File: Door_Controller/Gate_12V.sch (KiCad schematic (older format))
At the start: 6 parts

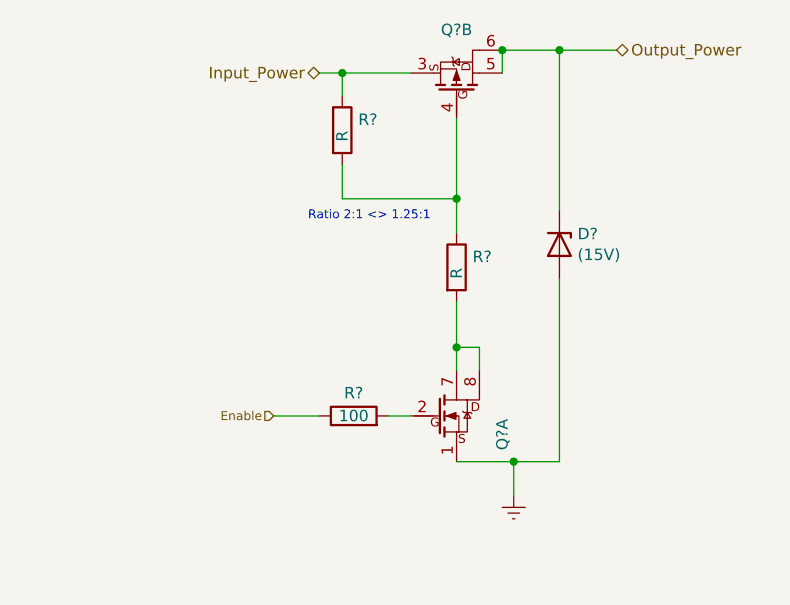
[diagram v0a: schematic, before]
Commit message: add filter caps to motor drive
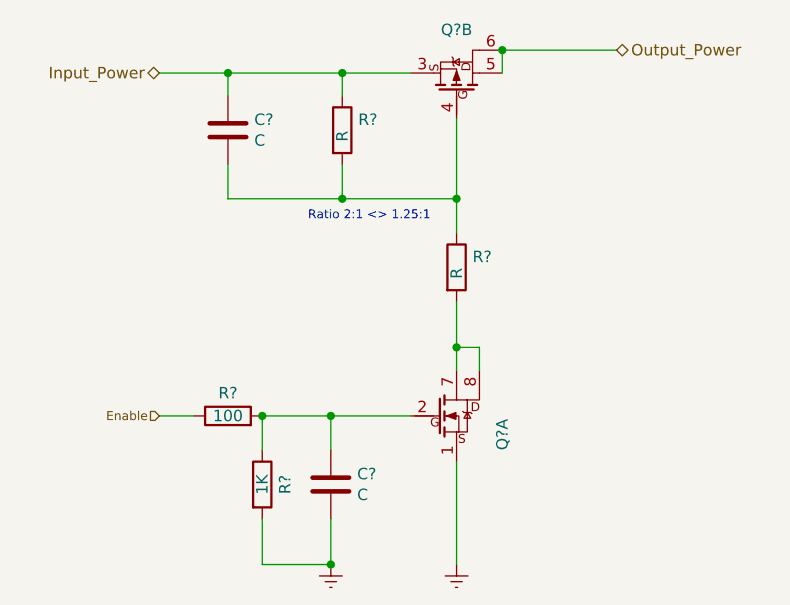
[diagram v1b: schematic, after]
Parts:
- removed D?: (15V), symbol Device:D_Zener
- added C? (x2): C, symbol Device:C
- added R?: 1K, symbol Device:R
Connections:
- net Earth: now also C?.2, R?.2
- net Input_Power: now also C?.1
- net at Q?.4, R?.1, R?.2: now also C?.2
- net at Q?.2, R?.2: now also C?.1, R?.1
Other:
- moved on the sheet: R?
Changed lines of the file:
@@
 $Descr A4 11693 8268
 encoding utf-8
-Sheet 7 14
+Sheet 8 14
 Title ""
 Date ""
@@
 Wire Wire Line
 	5200 2550 5200 2450
-Wire Wire Line
-	5200 2450 5450 2450
 Connection ~ 5200 2450
 $Comp
@@
 F 3 "~" H 4500 2800 50  0001 C CNN
 	1    4500 2800
+	1    0    0    -1
+$EndComp
+Text HLabel 3700 2550 0    50   BiDi ~ 0
+Input_Power
+Wire Wire Line
+	3700 2550 4000 2550
+Wire Wire Line
+	4500 2650 4500 2550
+Connection ~ 4500 2550
+Wire Wire Line
+	4500 2550 4800 2550
+Wire Wire Line
+	5000 3550 5000 3750
+Wire Wire Line
+	5100 3850 5100 3750
+Wire Wire Line
+	5100 3750 5000 3750
+Connection ~ 5000 3750
+Wire Wire Line
+	5000 3750 5000 3850
+Wire Wire Line
+	5000 2750 5000 3100
+Wire Wire Line
+	4500 2950 4500 3100
+Wire Wire Line
+	4500 3100 5000 3100
+Connection ~ 5000 3100
+Wire Wire Line
+	5000 3100 5000 3250
+$Comp
+L Device:R R?
+U 1 1 6066CE35
+P 5000 3400
+AR Path="/5FB4C28C/6066CE35" Ref="R?"  Part="1"
+AR Path="/5FB4C28C/606144ED/6066CE35" Ref="R?"  Part="1"
+AR Path="/5FB4C28C/60669CB5/6066CE35" Ref="R?"  Part="1"
+AR Path="/5FB4C28C/60BA7C5A/6066CE35" Ref="R?"  Part="1"
+F 0 "R?" H 5070 3446 50  0000 L CNN
+F 1 "R" V 5000 3350 50  0000 L CNN
+F 2 "" V 4930 3400 50  0001 C CNN
+F 3 "~" H 5000 3400 50  0001 C CNN
+	1    5000 3400
+	1    0    0    -1
+$EndComp
+Text Notes 4350 3200 0    39   ~ 0
+Ratio 2:1 <> 1.25:1
+Text HLabel 5700 2450 2    50   BiDi ~ 0
+Output_Power
+Wire Wire Line
+	5200 2450 5700 2450
+$Comp
+L power:Earth #PWR?
+U 1 1 6066DAA4
+P 5000 4700
+AR Path="/5FB4C28C/60669CB5/6066DAA4" Ref="#PWR?"  Part="1"
+AR Path="/5FB4C28C/60BA7C5A/6066DAA4" Ref="#PWR?"  Part="1"
+F 0 "#PWR?" H 5000 4450 50  0001 C CNN
+F 1 "Earth" H 5000 4550 50  0001 C CNN
+F 2 "" H 5000 4700 50  0001 C CNN
+F 3 "~" H 5000 4700 50  0001 C CNN
+	1    5000 4700
+	1    0    0    -1
+$EndComp
+Wire Wire Line
+	5000 4700 5000 4250
+$Comp
+L Device:C C?
+U 1 1 612B74C7
+P 4450 4350
+AR Path="/5FB4C28C/60669CB5/612B74C7" Ref="C?"  Part="1"
+AR Path="/5FB4C28C/60BA7C5A/612B74C7" Ref="C?"  Part="1"
+F 0 "C?" H 4565 4396 50  0000 L CNN
+F 1 "C" H 4565 4305 50  0000 L CNN
+F 2 "" H 4488 4200 50  0001 C CNN
+F 3 "~" H 4450 4350 50  0001 C CNN
+	1    4450 4350
 	1    0    0    -1
 $EndComp
@@
 	1    0    0    -1
 $EndComp
-Text HLabel 4400 2550 0    50   BiDi ~ 0
-Input_Power
-Wire Wire Line
-	4400 2550 4500 2550
-Wire Wire Line
-	4500 2650 4500 2550
-Connection ~ 4500 2550
-Wire Wire Line
-	4500 2550 4800 2550
-Wire Wire Line
-	5000 3550 5000 3750
-Wire Wire Line
-	5100 3850 5100 3750
-Wire Wire Line
-	5100 3750 5000 3750
-Connection ~ 5000 3750
-Wire Wire Line
-	5000 3750 5000 3850
-Wire Wire Line
-	5000 2750 5000 3100
-Wire Wire Line
-	4500 2950 4500 3100
-Wire Wire Line
-	4500 3100 5000 3100
-Connection ~ 5000 3100
-Wire Wire Line
-	5000 3100 5000 3250
-$Comp
-L Device:R R?
-U 1 1 6066CE35
-P 5000 3400
-AR Path="/5FB4C28C/6066CE35" Ref="R?"  Part="1"
-AR Path="/5FB4C28C/606144ED/6066CE35" Ref="R?"  Part="1"
-AR Path="/5FB4C28C/60669CB5/6066CE35" Ref="R?"  Part="1"
-AR Path="/5FB4C28C/60BA7C5A/6066CE35" Ref="R?"  Part="1"
-F 0 "R?" H 5070 3446 50  0000 L CNN
-F 1 "R" V 5000 3350 50  0000 L CNN
-F 2 "" V 4930 3400 50  0001 C CNN
-F 3 "~" H 5000 3400 50  0001 C CNN
-	1    5000 3400
-	1    0    0    -1
-$EndComp
-Text Notes 4350 3200 0    39   ~ 0
-Ratio 2:1 <> 1.25:1
+Wire Wire Line
+	3700 4050 3850 4050
+Text HLabel 3700 4050 0    39   Input ~ 0
+Enable
+Wire Wire Line
+	4150 4050 4450 4050
 $Comp
 L Device:R R?
 U 1 1 6066CE3D
-P 4550 4050
+P 4000 4050
 AR Path="/5FB4C28C/6066CE3D" Ref="R?"  Part="1"
 AR Path="/5FB4C28C/606144ED/6066CE3D" Ref="R?"  Part="1"
 AR Path="/5FB4C28C/60669CB5/6066CE3D" Ref="R?"  Part="1"
 AR Path="/5FB4C28C/60BA7C5A/6066CE3D" Ref="R?"  Part="1"
-F 0 "R?" V 4650 4050 50  0000 C CNN
-F 1 "100" V 4550 4050 50  0000 C CNN
-F 2 "" V 4480 4050 50  0001 C CNN
-F 3 "~" H 4550 4050 50  0001 C CNN
-	1    4550 4050
+F 0 "R?" V 4100 4050 50  0000 C CNN
+F 1 "100" V 4000 4050 50  0000 C CNN
+F 2 "" V 3930 4050 50  0001 C CNN
+F 3 "~" H 4000 4050 50  0001 C CNN
+	1    4000 4050
 	0    -1   -1   0
 $EndComp
-Wire Wire Line
-	4700 4050 4800 4050
-Text HLabel 4200 4050 0    39   Input ~ 0
-Enable
-Wire Wire Line
-	4200 4050 4400 4050
-$Comp
-L Device:D_Zener D?
-U 1 1 6066CE46
-P 5450 3300
-AR Path="/5FB4C28C/606144ED/6066CE46" Ref="D?"  Part="1"
-AR Path="/5FB4C28C/60669CB5/6066CE46" Ref="D?"  Part="1"
-AR Path="/5FB4C28C/60BA7C5A/6066CE46" Ref="D?"  Part="1"
-F 0 "D?" V 5404 3379 50  0000 L CNN
-F 1 "(15V)" V 5495 3379 50  0000 L CNN
-F 2 "" H 5450 3300 50  0001 C CNN
-F 3 "~" H 5450 3300 50  0001 C CNN
-	1    5450 3300
-	0    1    1    0
-$EndComp
-Wire Wire Line
-	5450 3150 5450 2450
-Wire Wire Line
-	5450 3450 5450 4250
-Wire Wire Line
-	5450 4250 5250 4250
 $Comp
 L power:Earth #PWR?
-U 1 1 6066DAA4
-P 5250 4400
-AR Path="/5FB4C28C/60669CB5/6066DAA4" Ref="#PWR?"  Part="1"
-AR Path="/5FB4C28C/60BA7C5A/6066DAA4" Ref="#PWR?"  Part="1"
-F 0 "#PWR?" H 5250 4150 50  0001 C CNN
-F 1 "Earth" H 5250 4250 50  0001 C CNN
-F 2 "" H 5250 4400 50  0001 C CNN
-F 3 "~" H 5250 4400 50  0001 C CNN
-	1    5250 4400
-	1    0    0    -1
-$EndComp
-Wire Wire Line
-	5250 4400 5250 4250
-Connection ~ 5250 4250
-Wire Wire Line
-	5250 4250 5000 4250
-Text HLabel 5700 2450 2    50   BiDi ~ 0
-Output_Power
-Wire Wire Line
-	5700 2450 5450 2450
-Connection ~ 5450 2450
+U 1 1 612BBD91
+P 4450 4700
+AR Path="/5FB4C28C/60669CB5/612BBD91" Ref="#PWR?"  Part="1"
+AR Path="/5FB4C28C/60BA7C5A/612BBD91" Ref="#PWR?"  Part="1"
+F 0 "#PWR?" H 4450 4450 50  0001 C CNN
+F 1 "Earth" H 4450 4550 50  0001 C CNN
+F 2 "" H 4450 4700 50  0001 C CNN
+F 3 "~" H 4450 4700 50  0001 C CNN
+	1    4450 4700
+	1    0    0    -1
+$EndComp
+Wire Wire Line
+	4450 4700 4450 4500
+Wire Wire Line
+	4450 4200 4450 4050
+Connection ~ 4450 4050
+Wire Wire Line
+	4450 4050 4800 4050
+$Comp
+L Device:C C?
+U 1 1 612BE1FE
+P 4000 2800
+AR Path="/5FB4C28C/60669CB5/612BE1FE" Ref="C?"  Part="1"
+AR Path="/5FB4C28C/60BA7C5A/612BE1FE" Ref="C?"  Part="1"
+F 0 "C?" H 4115 2846 50  0000 L CNN
+F 1 "C" H 4115 2755 50  0000 L CNN
+F 2 "" H 4038 2650 50  0001 C CNN
+F 3 "~" H 4000 2800 50  0001 C CNN
+	1    4000 2800
+	1    0    0    -1
+$EndComp
+Wire Wire Line
+	4000 2950 4000 3100
+Wire Wire Line
+	4000 3100 4500 3100
+Connection ~ 4500 3100
+Wire Wire Line
+	4000 2650 4000 2550
+Connection ~ 4000 2550
+Wire Wire Line
+	4000 2550 4500 2550
+$Comp
+L Device:R R?
+U 1 1 612E0ED5
+P 4150 4350
+AR Path="/5FB4C28C/612E0ED5" Ref="R?"  Part="1"
+AR Path="/5FB4C28C/606144ED/612E0ED5" Ref="R?"  Part="1"
+AR Path="/5FB4C28C/60669CB5/612E0ED5" Ref="R?"  Part="1"
+AR Path="/5FB4C28C/60BA7C5A/612E0ED5" Ref="R?"  Part="1"
+F 0 "R?" V 4250 4350 50  0000 C CNN
+F 1 "1K" V 4150 4350 50  0000 C CNN
+F 2 "" V 4080 4350 50  0001 C CNN
+F 3 "~" H 4150 4350 50  0001 C CNN
+	1    4150 4350
+	1    0    0    -1
+$EndComp
+Wire Wire Line
+	4150 4200 4150 4050
+Connection ~ 4150 4050
+Wire Wire Line
+	4150 4500 4150 4700
+Wire Wire Line
+	4150 4700 4450 4700
+Connection ~ 4450 4700
 $EndSCHEMATC
